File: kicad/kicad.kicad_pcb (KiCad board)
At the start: 2 copper layers, 100 x 100 mm, 110 parts, among them J101 DEBUG_LED_CONN, J102 EPD_SPI_CONN, J103 HPC_CONN, J104 USBC_CONN, J105 STORAGE_CONN, J106 MGMT_CONN, J107 GLOBAL_CONN, J108 INPUT_CONN, J201 USB_C_Receptacle_USB2.0_16P, J301 BATTERY_CONN, J501 MOTOR_P_SF, J502 MOTOR_N_SF, Q301 2N7002, Q401 SI1308EDL, SW701 PLACEHOLDER_BT1, SW702 PLACEHOLDER_BT2, SW703 PLACEHOLDER_BT3, SW704 BT1, SW705 BT2, SW706 BT3, SW707 BT4, U301 BQ25185, U302 TPS7A20, U501 DA7280, U601 M95P32

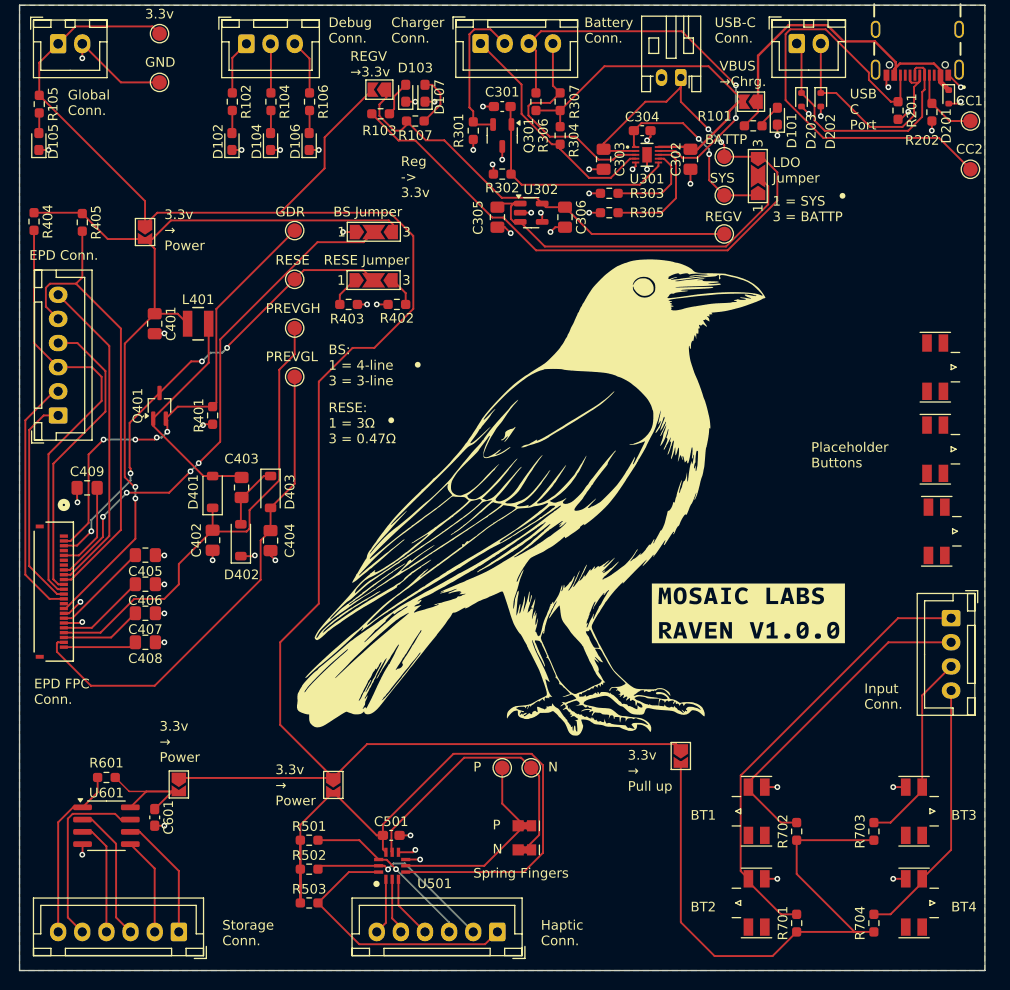
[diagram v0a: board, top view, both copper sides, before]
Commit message: Revision 2: Fix MOSFET pins and various changes
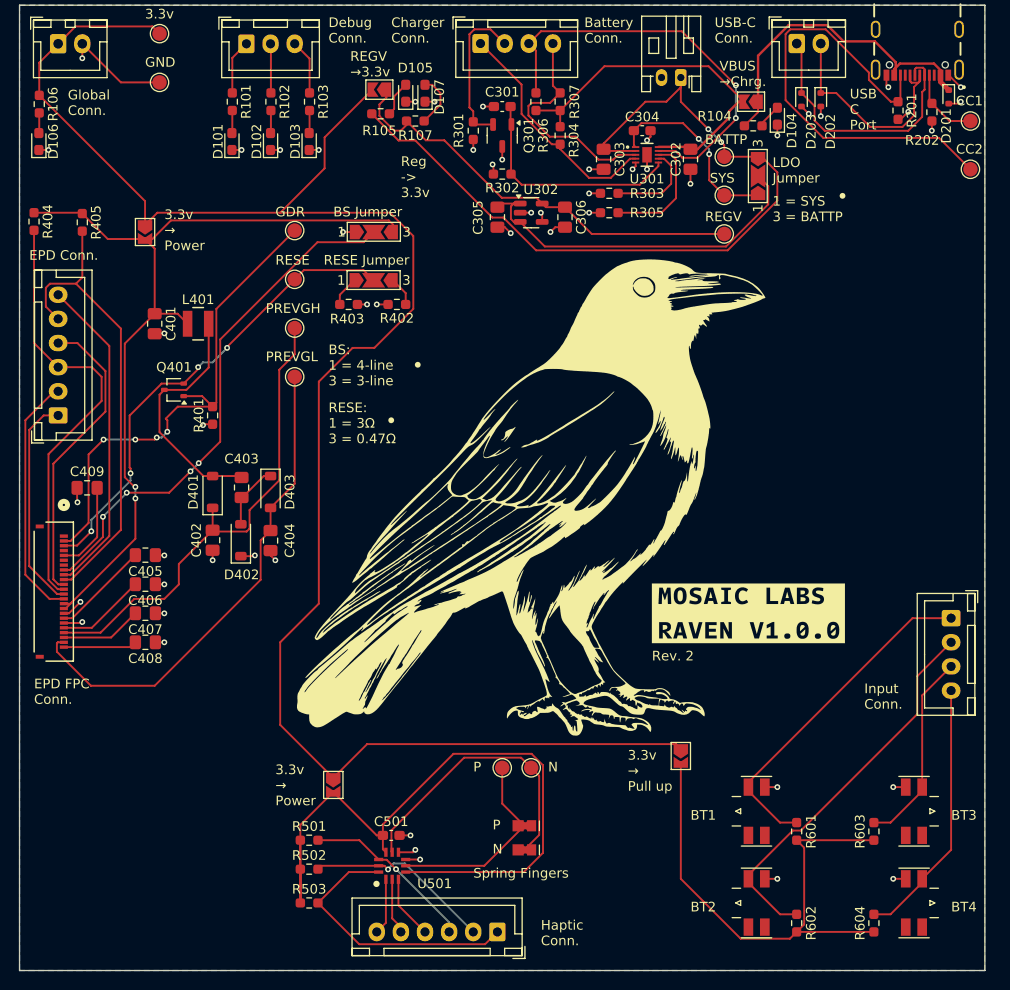
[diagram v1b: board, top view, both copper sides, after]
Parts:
- removed C601: 100nF, Capacitor_SMD:C_0603_1608Metric_Pad1.08x0.95mm_HandSolder
- removed the J105 at (109.5, 143.0)
- removed the JP102 at (109.5, 127.7)
- removed the R601 at (102.0, 127.0)
- removed SW701: PLACEHOLDER_BT1, Raven:PROTOTYPE_BUTTONS
- removed SW702: PLACEHOLDER_BT2, Raven:PROTOTYPE_BUTTONS
- removed SW703: PLACEHOLDER_BT3, Raven:PROTOTYPE_BUTTONS
- removed U601: M95P32, Package_SO:SOIC-8_3.9x4.9mm_P1.27mm
- Q401: value SI1308EDL -> Si1308EDL; footprint Package_TO_SOT_SMD:SOT-323_SC-70_Handsoldering -> Package_TO_SOT_SMD:SOT-323_SC-70
- moved R601 9.50 mm to (173.5, 132.6)
- moved R602 9.50 mm to (173.5, 142.1)
- moved SW601 9.50 mm to (169.3, 130.5)
- moved SW602 9.50 mm to (169.3, 140.0)
- moved Q401 2.23 mm to (109.0, 86.8), turned to 180 degrees
- renumbered D102 to D101, D104 to D102, D106 to D103, D101 to D104, D103 to D105, D105 to D106, J106 to J105, J107 to J106, J108 to J107, JP103 to JP102, JP104 to JP103, JP105 to JP104, JP106 to JP105, R102 to R101, R104 to R102, R106 to R103, R101 to R104, R103 to R105, R105 to R106, R701 to R601, R702 to R602, R703 to R603, R704 to R604, SW704 to SW601, SW705 to SW602, SW706 to SW603, SW707 to SW604, TP302 to TP301, TP303 to TP302, TP301 to TP303
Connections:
- Q401 pad 1: Net-(D401-A) -> /E-Paper Display/GDR
- Q401 pad 2: /E-Paper Display/GDR -> /E-Paper Display/RESE
- Q401 pad 3: /E-Paper Display/RESE -> Net-(D401-A)
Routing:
- net /Storage/HOLD_N: track 19.3 -> 0.00 mm
- net /Storage/S_N: track 18.3 -> 0.00 mm
- net /Storage/PWR: track 16.2 -> 0.00 mm
- net +3.3V: track 200.8 -> 184.8 mm
- net /Storage/Q: track 14.3 -> 0.00 mm
- net /Storage/C: track 13.0 -> 0.00 mm
- net /Storage/W_N: track 12.0 -> 0.00 mm
- net /Input/BT1: track 46.3 -> 35.3 mm
- net /Storage/D: track 10.1 -> 0.00 mm
- net /Input/BT2: track 34.2 -> 40.4 mm
- net /Input/PULL_UP: track 59.0 -> 53.0 mm
- net /E-Paper Display/GDR: track 48.1 -> 51.6 mm
- net GND: track 76.5 -> 74.4 mm, vias 54 -> 52
- net /E-Paper Display/PWR: track 87.6 -> 88.8 mm
- net Net-(D401-A): track 24.3 -> 25.1 mm
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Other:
- board text added: "Rev. 2"
- board text removed: "Placeholder Buttons"
- board text removed: "Storage Conn."

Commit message: Rev. 3: Fix issues
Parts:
- removed D104: VBUS_RLED, Diode_SMD:D_0603_1608Metric_Pad1.05x0.95mm_HandSolder
- removed D105: BATT_ALED, Diode_SMD:D_0603_1608Metric_Pad1.05x0.95mm_HandSolder
- removed D106: 3.3V_YLED, Diode_SMD:D_0603_1608Metric_Pad1.05x0.95mm_HandSolder
- removed D107: REGV_BLED, Diode_SMD:D_0603_1608Metric_Pad1.05x0.95mm_HandSolder
- removed R104: 150, Resistor_SMD:R_0603_1608Metric_Pad0.98x0.95mm_HandSolder
- removed R105: 82, Resistor_SMD:R_0603_1608Metric_Pad0.98x0.95mm_HandSolder
- removed R106: 68, Resistor_SMD:R_0603_1608Metric_Pad0.98x0.95mm_HandSolder
- removed R107: 5.1, Resistor_SMD:R_0603_1608Metric_Pad0.98x0.95mm_HandSolder
- D101: value DEBUG_RLED -> NOTIFY_RLED
- D102: value DEBUG_GLED -> NOTIFY_GLED
- D103: value DEBUG_BLED -> NOTIFY_BLED
- EPD_FPC401: footprint Raven:CONN24x1_FH34SRJ-24S-0.5SH50_HIR -> Raven:CONN_F3311A7H121024E200_AMP
- J101: value DEBUG_LED_CONN -> NOTIFY_LED_CONN
- R101, R102: value 68 -> 560
- R103: value 5.1 -> 560
- moved G*** 2.38 mm to (148.8, 98.5)
- moved EPD_FPC401 0.64 mm to (95.9, 107.7)
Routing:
- net +BATT: track 84.6 -> 29.0 mm
- net Net-(D107-A): track 5.55 -> 0.00 mm
- net GND: track 74.4 -> 70.3 mm, vias 52 -> 48
- net Net-(D105-A): track 3.70 -> 0.00 mm
- net VBUS: track 34.8 -> 31.7 mm
- net Net-(D104-A): track 2.53 -> 0.00 mm
- net Net-(D106-A): track 2.10 -> 0.00 mm
- net +3.3V: track 184.8 -> 183.1 mm
- net REGV: track 44.9 -> 43.7 mm
- net /Haptics/SCL: track 19.6 -> 19.1 mm, vias 1 -> 2
- net /Haptics/SDA: vias 1 -> 2
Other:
- board text added: "Notify Conn."
- board text added: "Rev. 3"
- board text removed: "Debug Conn."
- board text removed: "Rev. 2"

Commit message: Minor revisions for haptics and PCB
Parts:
- removed J501: MOTOR_P_SF, Raven:TE_2329497-2
- removed J502: MOTOR_N_SF, Raven:TE_2329497-2
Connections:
- net /Haptics/OUTN_T renamed Net-(U501-OUTN)
- net /Haptics/OUTP_T renamed Net-(U501-OUTP)
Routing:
- net Net-(U501-OUTN): track 29.8 -> 20.3 mm
- net Net-(U501-OUTP): track 21.0 -> 15.3 mm
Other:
- board text added: "Rev. 4"
- board text removed: "Rev. 3"
- board text removed: "Spring Fingers"

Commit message: Begin PCB, update footprints
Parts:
- removed J101: NOTIFY_LED_CONN, Connector_JST:JST_XH_B3B-XH-A_1x03_P2.50mm_Vertical
- removed J102: EPD_SPI_CONN, Connector_JST:JST_XH_B6B-XH-A_1x06_P2.50mm_Vertical
- removed J103: HPC_CONN, Connector_JST:JST_XH_B6B-XH-A_1x06_P2.50mm_Vertical
- removed J104: USBC_CONN, Connector_JST:JST_XH_B2B-XH-A_1x02_P2.50mm_Vertical
- removed J105: MGMT_CONN, Connector_JST:JST_XH_B4B-XH-A_1x04_P2.50mm_Vertical
- removed J106: GLOBAL_CONN, Connector_JST:JST_XH_B2B-XH-A_1x02_P2.50mm_Vertical
- removed J107: INPUT_CONN, Connector_JST:JST_XH_B4B-XH-A_1x04_P2.50mm_Vertical
- removed JP101: EPD_PWR_JP, Jumper:SolderJumper-2_P1.3mm_Open_TrianglePad1.0x1.5mm
- removed JP102: HPC_PWR_JP, Jumper:SolderJumper-2_P1.3mm_Open_TrianglePad1.0x1.5mm
- removed JP103: INPUT_PULL_JP, Jumper:SolderJumper-2_P1.3mm_Open_TrianglePad1.0x1.5mm
- removed JP104: CHRG_JP, Jumper:SolderJumper-2_P1.3mm_Open_TrianglePad1.0x1.5mm
- removed JP105: LDO_JP, Jumper:SolderJumper-2_P1.3mm_Open_TrianglePad1.0x1.5mm
- removed JP301: LDO_JP, Jumper:SolderJumper-3_P2.0mm_Open_TrianglePad1.0x1.5mm_NumberLabels
- removed JP401: BS_L_JP, Jumper:SolderJumper-3_P2.0mm_Open_TrianglePad1.0x1.5mm_NumberLabels
- removed JP402: RESE_JP, Jumper:SolderJumper-3_P2.0mm_Open_TrianglePad1.0x1.5mm_NumberLabels
- removed R405: 100k, Resistor_SMD:R_0603_1608Metric_Pad0.98x0.95mm_HandSolder
- removed TP101: 3V3_TEST, TestPoint:TestPoint_Pad_D1.5mm
- removed TP102: GND_TEST, TestPoint:TestPoint_Pad_D1.5mm
- removed TP201: CC1_TEST, TestPoint:TestPoint_Pad_D1.5mm
- removed TP202: CC2_TEST, TestPoint:TestPoint_Pad_D1.5mm
- removed TP401: GDR_TEST, TestPoint:TestPoint_Pad_D1.5mm
- removed TP402: RESE_TEST, TestPoint:TestPoint_Pad_D1.5mm
- removed TP403: PREVGH_TEST, TestPoint:TestPoint_Pad_D1.5mm
- removed TP404: PREVGL_TEST, TestPoint:TestPoint_Pad_D1.5mm
- added C701: 100pF, Capacitor_SMD:C_0402_1005Metric, F.Cu at (261.3, 25.2)
- added C702: 100nF, Capacitor_SMD:C_0603_1608Metric_Pad1.08x0.95mm_HandSolder, F.Cu at (247.4, 21.7)
- added C703: 100nF, Capacitor_SMD:C_0603_1608Metric_Pad1.08x0.95mm_HandSolder, F.Cu at (247.4, 24.2)
- added C704: 1.2pF, Capacitor_SMD:C_0402_1005Metric, F.Cu at (261.3, 27.2)
- added C707: 4.7uF, Capacitor_SMD:C_0805_2012Metric_Pad1.18x1.45mm_HandSolder, F.Cu at (258.1, 32.2)
- added C708: 100nF, Capacitor_SMD:C_0603_1608Metric_Pad1.08x0.95mm_HandSolder, F.Cu at (247.4, 26.7)
- added C709: 1uF, Capacitor_SMD:C_0805_2012Metric_Pad1.18x1.45mm_HandSolder, F.Cu at (258.1, 35.2)
- added C710: 10nF, Capacitor_SMD:C_0603_1608Metric_Pad1.08x0.95mm_HandSolder, F.Cu at (247.4, 29.2)
- added C711: 100nF, Capacitor_SMD:C_0603_1608Metric_Pad1.08x0.95mm_HandSolder, F.Cu at (247.4, 31.7)
- added C712: 100nF, Capacitor_SMD:C_0603_1608Metric_Pad1.08x0.95mm_HandSolder, F.Cu at (247.4, 34.2)
- added C713: 100nF, Capacitor_SMD:C_0603_1608Metric_Pad1.08x0.95mm_HandSolder, F.Cu at (247.4, 36.7)
- added C714: 100nF, Capacitor_SMD:C_0603_1608Metric_Pad1.08x0.95mm_HandSolder, F.Cu at (247.4, 39.3)
- added L701: 3.6nH, Capacitor_SMD:C_0402_1005Metric_Pad0.74x0.62mm_HandSolder, F.Cu at (261.4, 29.1)
- added Q701: 2N7002, Package_TO_SOT_SMD:SOT-23-3, F.Cu at (258.2, 39.1)
- added R104: 0, Resistor_SMD:R_0603_1608Metric_Pad0.98x0.95mm_HandSolder, F.Cu at (267.3, 21.7)
- added R105: 560, Resistor_SMD:R_0603_1608Metric_Pad0.98x0.95mm_HandSolder, F.Cu at (267.3, 24.2)
- added R106: 560, Resistor_SMD:R_0603_1608Metric_Pad0.98x0.95mm_HandSolder, F.Cu at (267.3, 26.7)
- added R107: 560, Resistor_SMD:R_0603_1608Metric_Pad0.98x0.95mm_HandSolder, F.Cu at (267.3, 29.2)
- added R108: 0, Resistor_SMD:R_0603_1608Metric_Pad0.98x0.95mm_HandSolder, F.Cu at (267.3, 31.7)
- added R701: 100k, Resistor_SMD:R_0603_1608Metric_Pad0.98x0.95mm_HandSolder, F.Cu at (247.4, 41.8)
- added R702: 10k, Resistor_SMD:R_0603_1608Metric_Pad0.98x0.95mm_HandSolder, F.Cu at (247.4, 44.3)
- added SW101: PWR_SWITCH, Raven:SSSS811101, F.Cu at (67.3, 111.0)
- added TP701: NRST_PAD, TestPoint:TestPoint_Pad_D1.0mm, F.Cu at (251.1, 32.2)
- added TP702: BOOT0_PAD, TestPoint:TestPoint_Pad_D1.0mm, F.Cu at (251.1, 35.3)
- added TP703: FLASH_GND, TestPoint:TestPoint_Pad_D1.0mm, F.Cu at (251.1, 38.3)
- added TP704: FLASH_DIO, TestPoint:TestPoint_Pad_D1.0mm, F.Cu at (251.1, 41.4)
- added TP705: FLASH_CLK, TestPoint:TestPoint_Pad_D1.0mm, F.Cu at (254.1, 32.2)
- added TP706: FLASH_RST, TestPoint:TestPoint_Pad_D1.0mm, F.Cu at (254.1, 35.3)
- added TP707: FLASH_VDD, TestPoint:TestPoint_Pad_D1.0mm, F.Cu at (254.1, 38.3)
- added U701: STM32WB55RGVx, Package_DFN_QFN:QFN-68-1EP_8x8mm_P0.4mm_EP6.4x6.4mm, F.Cu at (56.2, 106.2)
- added U702: MLPF-WB55-01E3, Raven:MLPF-WB55-01E3, F.Cu at (261.5, 22.3)
- added Y702: 32M, Raven:XTAL_ECS-160-9-37-CKM-TR, F.Cu at (258.0, 43.0)
- D101: value NOTIFY_RLED -> NOTIFY_BLED
- D103: value NOTIFY_BLED -> NOTIFY_RLED
- R101, R102, R103: value 560 -> 0
- R201: footprint Resistor_SMD:R_0603_1608Metric_Pad0.98x0.95mm_HandSolder -> Resistor_SMD:R_0402_1005Metric
- R202: footprint Resistor_SMD:R_0603_1608Metric_Pad0.98x0.95mm_HandSolder -> Resistor_SMD:R_0402_1005Metric_Pad0.72x0.64mm_HandSolder
- R402: value 0.47 -> 3
- R403: value 3 -> 100k
- SW601, SW604: footprint Raven:PROTOTYPE_BUTTONS -> Raven:EVQPUA
- SW602: value BT2 -> BT3; footprint Raven:PROTOTYPE_BUTTONS -> Raven:EVQPUA
- SW603: value BT3 -> BT2; footprint Raven:PROTOTYPE_BUTTONS -> Raven:EVQPUA
- TP301, TP302, TP303: footprint TestPoint:TestPoint_Pad_D1.5mm -> TestPoint:TestPoint_Pad_D1.0mm
- TP501: value OUTP_TEST -> OUTP_PAD; footprint TestPoint:TestPoint_Pad_D1.5mm -> TestPoint:TestPoint_Pad_D1.0mm
- TP502: value OUTN_TEST -> OUTN_PAD; footprint TestPoint:TestPoint_Pad_D1.5mm -> TestPoint:TestPoint_Pad_D1.0mm
- moved J201 159.3 mm to (39.0, 111.0), turned to -90 degrees
- moved SW601 134.0 mm to (39.9, 95.9)
- moved SW602 130.9 mm to (39.8, 121.1)
- moved SW603 122.7 mm to (66.6, 100.8)
- moved SW604 119.7 mm to (66.6, 126.6)
- moved EPD_FPC401 44.6 mm to (53.0, 120.0), turned to 0 degrees
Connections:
- net /USB-C/DM renamed /Microcontroller/DM
- net /USB-C/DP renamed /Microcontroller/DP
- C305 pad 1: Net-(JP301-C) -> /Battery Management/SYS_T
- EPD_FPC401 pad 8: /E-Paper Display/BS -> GND
- R101 pad 1: Net-(J101-Pin_1) -> /Input/PULL_UP
- R101 pad 2: Net-(D101-A) -> +3.3V
- R102 pad 1: Net-(J101-Pin_2) -> VBUS
- R102 pad 2: Net-(D102-A) -> /Battery Management/CHRG
- R103 pad 1: Net-(J101-Pin_3) -> +3.3V
- R103 pad 2: Net-(D103-A) -> /Microcontroller/SMPS
- R304 pad 2: /Battery Management/CE_N -> GND
- R402 pad 1: Net-(JP402-B) -> /E-Paper Display/RESE
- R403 pad 1: Net-(JP402-A) -> /E-Paper Display/PWR
- R403 pad 2: GND -> /E-Paper Display/CS_N
- R404 pad 2: /E-Paper Display/CS_N -> /E-Paper Display/RES_N
- R602 pad 2: /Input/BT2 -> /Input/BT3
- R603 pad 2: /Input/BT3 -> /Input/BT2
- SW602 pad 2: /Input/BT2 -> /Input/BT3
- SW603 pad 2: /Input/BT3 -> /Input/BT2
- U301 pad 4: /Battery Management/CE_N -> GND
- U302 pad 1: Net-(JP301-C) -> /Battery Management/SYS_T
- U302 pad 3: Net-(JP301-C) -> /Battery Management/SYS_T
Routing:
- net GND: track 70.3 -> 148.1 mm, vias 48 -> 51
- net /E-Paper Display/BS: track 54.1 -> 0.00 mm, vias 4 -> 0
- net /E-Paper Display/RES_N: track 48.2 -> 93.7 mm
- net /E-Paper Display/CS_N: track 45.4 -> 1.00 mm, vias 0 -> 1
- net Net-(JP301-C): track 37.9 -> 0.00 mm
- net /Battery Management/SYS_T: track 19.9 -> 57.8 mm
- net /Battery Management/CE_N: track 24.7 -> 0.00 mm
- net /Input/BT3: track 20.5 -> 40.4 mm
- net /Input/BT2: track 40.4 -> 20.5 mm
- net +3.3V: track 183.1 -> 188.8 mm
- net Net-(J101-Pin_3): track 5.73 -> 0.00 mm
- net Net-(J101-Pin_1): track 5.69 -> 0.00 mm
- net /Input/PULL_UP: track 53.0 -> 58.7 mm
- net VBUS: track 31.7 -> 36.8 mm
- net Net-(J101-Pin_2): track 5.10 -> 0.00 mm
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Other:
- board size 100 x 100 mm -> 155.7 x 100 mm

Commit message: PCB progress
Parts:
- removed C713, C714: 100nF, Capacitor_SMD:C_0603_1608Metric_Pad1.08x0.95mm_HandSolder
- removed G*** (x2): LOGO, LOGO
- removed Y702: 32M, Raven:XTAL_ECS-160-9-37-CKM-TR
- added AE701: MEANDER_ANT, Raven:AN3359_ANT, F.Cu at (247.5, 81.0)
- added C705: 1uF, Capacitor_SMD:C_0402_1005Metric, F.Cu at (172.3, 124.5)
- added C706: 100nF, Capacitor_SMD:C_0402_1005Metric, F.Cu at (172.3, 126.4)
- added D104: LED_F2, Diode_SMD:D_0603_1608Metric, F.Cu at (153.6, 129.1)
- added R109: 0, Resistor_SMD:R_0402_1005Metric, F.Cu at (201.0, 134.8)
- added Y701: 32M, Raven:XTAL_ECS-160-9-37-CKM-TR, F.Cu at (149.0, 114.5)
- C301, C304, C501, C702, C708, C712: footprint Capacitor_SMD:C_0603_1608Metric_Pad1.08x0.95mm_HandSolder -> Capacitor_SMD:C_0402_1005Metric
- C302, C303, C305, C306, C402, C404, C405, C406, C407, C408, C409: footprint Capacitor_SMD:C_0805_2012Metric_Pad1.18x1.45mm_HandSolder -> Capacitor_SMD:C_0402_1005Metric
- C401, C403: footprint Capacitor_SMD:C_0805_2012Metric_Pad1.18x1.45mm_HandSolder -> Capacitor_SMD:C_0805_2012Metric
- C701: value 100pF -> 1.2pF
- C703: value 100nF -> 4.7uF; footprint Capacitor_SMD:C_0603_1608Metric_Pad1.08x0.95mm_HandSolder -> Capacitor_SMD:C_0402_1005Metric
- C704: value 1.2pF -> 100nF
- C707: value 4.7uF -> 10nF; footprint Capacitor_SMD:C_0805_2012Metric_Pad1.18x1.45mm_HandSolder -> Capacitor_SMD:C_0402_1005Metric
- C709: value 1uF -> 100nF; footprint Capacitor_SMD:C_0805_2012Metric_Pad1.18x1.45mm_HandSolder -> Capacitor_SMD:C_0402_1005Metric
- C710: value 10nF -> 100nF; footprint Capacitor_SMD:C_0603_1608Metric_Pad1.08x0.95mm_HandSolder -> Capacitor_SMD:C_0402_1005Metric
- C711: value 100nF -> 100pF; footprint Capacitor_SMD:C_0603_1608Metric_Pad1.08x0.95mm_HandSolder -> Capacitor_SMD:C_0402_1005Metric
- D101: value NOTIFY_BLED -> LED_PWR; footprint Diode_SMD:D_0603_1608Metric_Pad1.05x0.95mm_HandSolder -> Diode_SMD:D_0603_1608Metric
- D102: value NOTIFY_GLED -> LED_BATT; footprint Diode_SMD:D_0603_1608Metric_Pad1.05x0.95mm_HandSolder -> Diode_SMD:D_0603_1608Metric
- D103: value NOTIFY_RLED -> LED_F1; footprint Diode_SMD:D_0603_1608Metric_Pad1.05x0.95mm_HandSolder -> Diode_SMD:D_0603_1608Metric
- J301: footprint Connector_JST:JST_PH_S2B-PH-K_1x02_P2.00mm_Horizontal -> Raven:CUSTOM_BATT_CONN
- L701: footprint Capacitor_SMD:C_0402_1005Metric_Pad0.74x0.62mm_HandSolder -> Inductor_SMD:L_0402_1005Metric
- R101, R102, R103, R104, R105, R106, R107, R301, R302, R303, R304, R305, R306, R307, R401, R402, R403, R404, R501, R502, R503, R601, R602, R603, R604, R701, R702: footprint Resistor_SMD:R_0603_1608Metric_Pad0.98x0.95mm_HandSolder -> Resistor_SMD:R_0402_1005Metric
- R108: value 0 -> 560; footprint Resistor_SMD:R_0603_1608Metric_Pad0.98x0.95mm_HandSolder -> Resistor_SMD:R_0402_1005Metric
- R202: footprint Resistor_SMD:R_0402_1005Metric_Pad0.72x0.64mm_HandSolder -> Resistor_SMD:R_0402_1005Metric
- TP701: value NRST_PAD -> BOOT0_PAD
- TP702: value BOOT0_PAD -> NRST_PAD
- U701: value STM32WB55RGVx -> MLPF-WB55-01E3; footprint Package_DFN_QFN:QFN-68-1EP_8x8mm_P0.4mm_EP6.4x6.4mm -> Raven:MLPF-WB55-01E3
- U702: value MLPF-WB55-01E3 -> STM32WB55RGVx; footprint Raven:MLPF-WB55-01E3 -> Package_DFN_QFN:QFN-68-1EP_8x8mm_P0.4mm_EP6.4x6.4mm
- moved U702 148.9 mm to (142.1, 111.2)
- moved U701 134.8 mm to (188.6, 131.6)
- moved C702 129.8 mm to (134.9, 86.5), turned to 90 degrees
- moved C703 126.4 mm to (137.4, 86.5), turned to 90 degrees
- moved C708 123.0 mm to (139.9, 86.5), turned to 90 degrees
- moved C710 119.6 mm to (142.4, 86.5), turned to 90 degrees
- moved C711 116.2 mm to (144.9, 86.5), turned to 90 degrees
- moved C712 112.8 mm to (147.5, 86.5), turned to 90 degrees
- moved R701 102.6 mm to (155.0, 86.5), turned to 90 degrees
- moved R702 99.3 mm to (157.5, 86.5), turned to 90 degrees
- moved SW101 89.6 mm to (156.8, 116.1)
- moved EPD_FPC401 89.5 mm to (142.5, 123.8)
- moved SW602 89.3 mm to (129.1, 124.4)
- moved SW601 89.3 mm to (129.1, 95.2)
- moved SW604 89.2 mm to (155.8, 129.6)
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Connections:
- C701 pad 1: /Microcontroller/SMPS -> Net-(AE701-A)
- C704 pad 1: Net-(AE701-A) -> /Microcontroller/SMPS
- C708 pad 1: GND -> /Microcontroller/SMPS
- C708 pad 2: /Microcontroller/SMPS -> GND
- C712 pad 1: /Microcontroller/SMPS -> GND
- C712 pad 2: GND -> /Microcontroller/SMPS
- L701 pad 2: Net-(U702-OUT) -> Net-(U701-OUT)
- R105 pad 1: /Microcontroller/LED_RED -> +3V3
- R106 pad 1: /Microcontroller/LED_BLUE -> /Microcontroller/LED_BATT
- R107 pad 1: /Microcontroller/LED_GREEN -> /Microcontroller/LED_F1
- R108 pad 1: +3.3V -> /Microcontroller/LED_F2
- R108 pad 2: /Haptics/PWR -> Net-(D104-A)
- TP701 pad 1: /Microcontroller/NRST -> Net-(Q701-D)
- TP702 pad 1: Net-(Q701-D) -> /Microcontroller/NRST
- U701 pad 1: /Microcontroller/SMPS -> Net-(U701-OUT)
- U701 pad 2: unconnected-(U701-PC13-Pad2) -> GND
- U701 pad 3: unconnected-(U701-PC14-Pad3) -> Net-(U701-IN)
- U701 pad 4: unconnected-(U701-PC15-Pad4) -> GND
- U701 pad 5: unconnected-(U701-PH3-Pad5) -> GND
- U701 pad 6: /Haptics/SCL -> GND
- U702 pad 1: Net-(U702-OUT) -> /Microcontroller/SMPS
- U702 pad 2: GND -> unconnected-(U702-PC13-Pad2)
- U702 pad 3: Net-(U701-RF1) -> unconnected-(U702-PC14-Pad3)
- U702 pad 4: GND -> unconnected-(U702-PC15-Pad4)
- U702 pad 5: GND -> unconnected-(U702-PH3-Pad5)
- U702 pad 6: GND -> /Haptics/SCL
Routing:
- net +3.3V: track 188.8 -> 0.00 mm
- net GND: track 148.1 -> 6.08 mm, vias 51 -> 1
- net /E-Paper Display/RES_N: track 93.7 -> 0.00 mm
- net /E-Paper Display/PWR: track 91.9 -> 0.00 mm, vias 2 -> 0
- net /Haptics/PWR: track 77.2 -> 0.00 mm
- net /Input/PULL_UP: track 58.7 -> 0.00 mm
- net /Battery Management/SYS_T: track 57.8 -> 0.00 mm, vias 2 -> 0
- net /E-Paper Display/RESE: track 52.4 -> 0.00 mm, vias 4 -> 0
- net /E-Paper Display/GDR: track 51.6 -> 0.00 mm, vias 4 -> 0
- net /E-Paper Display/PREVGL: track 51.2 -> 0.00 mm
- net /E-Paper Display/PREVGH: track 50.1 -> 0.00 mm
- net /USB-C/CC2_T: track 47.2 -> 0.00 mm
- net REGV: track 43.7 -> 0.00 mm
- net /Battery Management/STAT1: track 43.2 -> 0.00 mm, vias 2 -> 0
- net /Input/BT3: track 40.4 -> 0.00 mm
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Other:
- board size 155.7 x 100 mm -> 31.8 x 37.3 mm
- board text removed: "1 = SYS 3 = BATTP"
- board text removed: "3.3v"
- board text removed: "3.3v → Power"
- board text removed: "3.3v → Pull up"
- board text removed: "BS Jumper"
- board text removed: "BS: 1 = 4-line 3 = 3-line"
- board text removed: "BT1"
- board text removed: "BT2"
- board text removed: "BT3"
- board text removed: "BT4"
- board text removed: "Battery Conn."
- board text removed: "CC1"
- board text removed: "CC2"
- board text removed: "Charger Conn."
- board text removed: "EPD Conn."
- board text removed: "EPD FPC Conn."
- board text removed: "GDR"
- board text removed: "GND"
- board text removed: "Global Conn."
- board text removed: "Haptic Conn."
- board text removed: "Input Conn."
- board text removed: "LDO Jumper"
- board text removed: "N"
- board text removed: "Notify Conn."
- board text removed: "P"
- board text removed: "PREVGH"
- board text removed: "PREVGL"
- board text removed: "REGV →3.3v"
- board text removed: "RESE"
- board text removed: "RESE Jumper"
- board text removed: "RESE: 1 = 3Ω 3 = 0.47Ω"
- board text removed: "Reg -> 3.3v"
- board text removed: "Rev. 4"
- board text removed: "USB C Port"
- board text removed: "USB-C Conn."
- board text removed: "VBUS →Chrg."
